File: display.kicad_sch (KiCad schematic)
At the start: 38 parts, among them J301 ConnectorLCDFrontLight, J302 FPC24(0.5MM), J303 FPC10(0.5MM), Q301 2N7002, Q302 2N7002, Q303 AO3401A

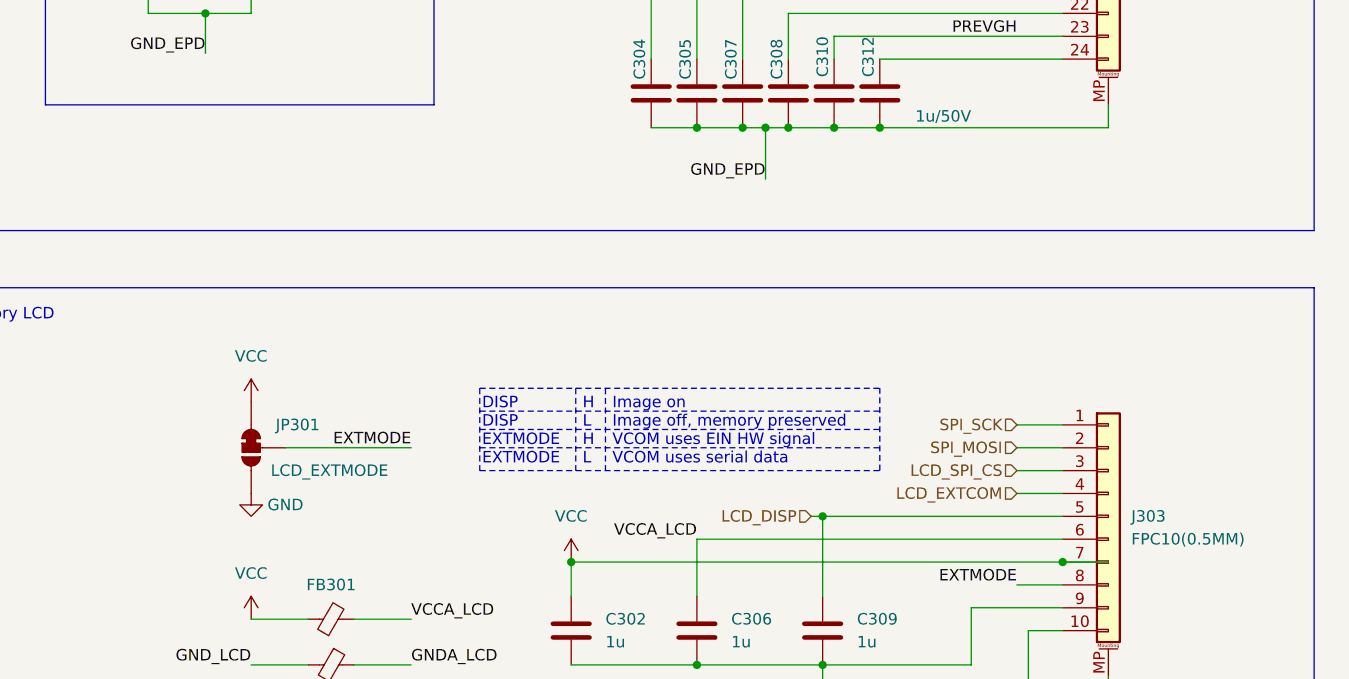
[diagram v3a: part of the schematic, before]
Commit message: schematic: add placeholders for the actual displays
Also fixup GND_LCD for Extmode SolderJumper.
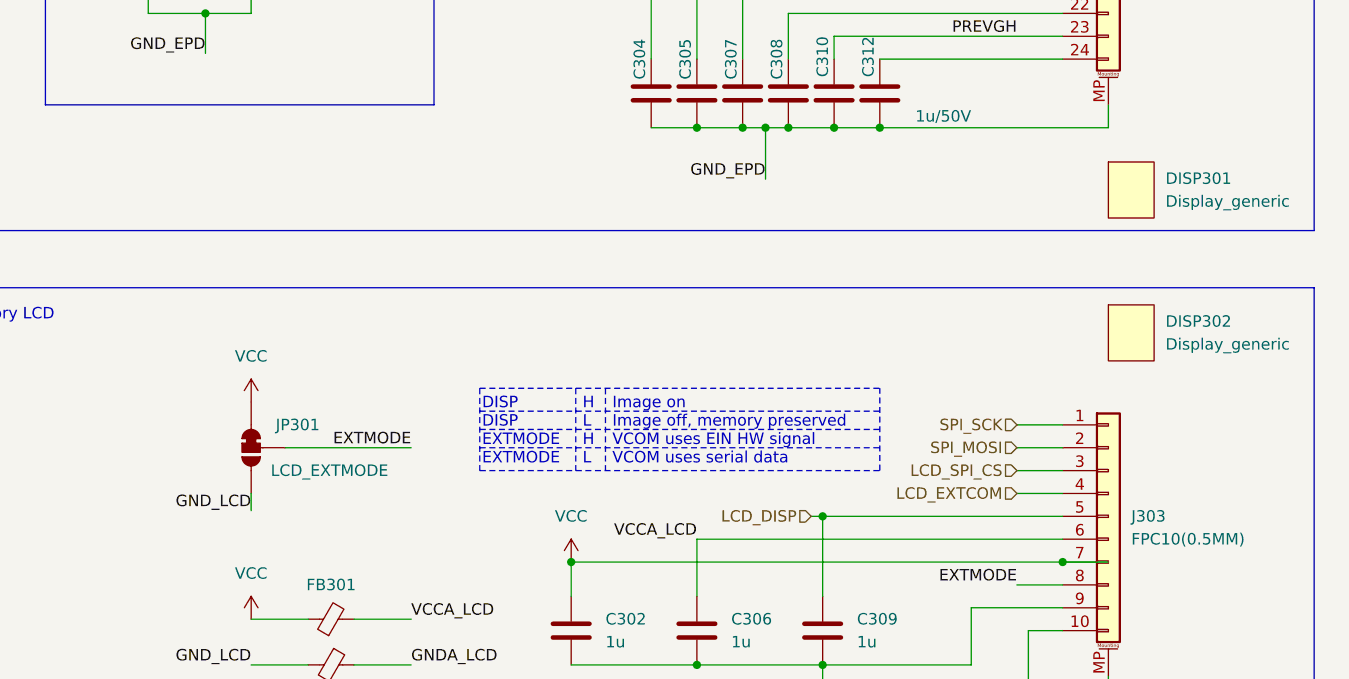
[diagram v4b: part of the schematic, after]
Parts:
- added DISP301, DISP302: Display_generic, project-lib:154_Epaper_Display, symbol project-lib:Display_generic
- J301: JLCPCB (none) -> C11047
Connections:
- net GND: no longer JP301.3 (B)
- net LCD_CURRENT_SENSE: now also JP301.3 (B)
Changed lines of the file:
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@@
+    (stroke (width 0) (type default) (color 0 0 0 0))
+  )
+  (wire (pts (xy 160.02 133.35) (xy 160.02 135.255))
     (stroke (width 0) (type default) (color 0 0 0 0))
   )
@@
   )
   (label "EXTMODE" (at 177.8 128.27 180)
+    (effects (font (size 1.27 1.27)) (justify right bottom))
+  )
+  (label "GND_LCD" (at 160.02 135.255 180)
     (effects (font (size 1.27 1.27)) (justify right bottom))
   )
@@
     )
     (property "Datasheet" "" (id 3) (at 160.02 123.19 0)
-      (effects (font (size 1.27 1.27)) hide)
-    )
-    (pin "1")
-  )
-  (symbol (lib_id "power:GND") (at 160.02 133.35 0) (unit 1)
-    (in_bom yes) (on_board yes)
-    (property "Reference" "#PWR0309" (id 0) (at 160.02 139.7 0)
-      (effects (font (size 1.27 1.27)) hide)
-    )
-    (property "Value" "GND" (id 1) (at 163.83 134.62 0))
-    (property "Footprint" "" (id 2) (at 160.02 133.35 0)
-      (effects (font (size 1.27 1.27)) hide)
-    )
-    (property "Datasheet" "" (id 3) (at 160.02 133.35 0)
       (effects (font (size 1.27 1.27)) hide)
     )
@@
       (effects (font (size 1.27 1.27)) hide)
     )
+    (property "JLCPCB" "C11047" (id 4) (at 102.235 139.7 0)
+      (effects (font (size 1.27 1.27)) hide)
+    )
     (pin "1")
     (pin "2")
@@
     (pin "1")
   )
+  (symbol (lib_id "project-lib:Display_generic") (at 257.81 116.205 0) (unit 1)
+    (in_bom no) (on_board yes) (fields_autoplaced)
+    (property "Reference" "DISP302" (id 0) (at 261.62 114.2364 0)
+      (effects (font (size 1.27 1.27)) (justify left))
+    )
+    (property "Value" "Display_generic" (id 1) (at 261.62 116.7764 0)
+      (effects (font (size 1.27 1.27)) (justify left))
+    )
+    (property "Footprint" "project-lib:154_Epaper_Display" (id 2) (at 257.81 116.205 0)
+      (effects (font (size 1.27 1.27)) hide)
+    )
+    (property "Datasheet" "" (id 3) (at 257.81 116.205 0)
+      (effects (font (size 1.27 1.27)) hide)
+    )
+  )
   (symbol (lib_id "Device:D") (at 171.45 67.31 0) (unit 1)
     (in_bom yes) (on_board yes)
@@
     (pin "1")
   )
+  (symbol (lib_id "project-lib:Display_generic") (at 257.81 100.33 0) (unit 1)
+    (in_bom no) (on_board yes) (fields_autoplaced)
+    (property "Reference" "DISP301" (id 0) (at 261.62 98.3614 0)
+      (effects (font (size 1.27 1.27)) (justify left))
+    )
+    (property "Value" "Display_generic" (id 1) (at 261.62 100.9014 0)
+      (effects (font (size 1.27 1.27)) (justify left))
+    )
+    (property "Footprint" "project-lib:154_Epaper_Display" (id 2) (at 257.81 100.33 0)
+      (effects (font (size 1.27 1.27)) hide)
+    )
+    (property "Datasheet" "" (id 3) (at 257.81 100.33 0)
+      (effects (font (size 1.27 1.27)) hide)
+    )
+  )
   (symbol (lib_id "Transistor_FET:2N7002") (at 90.17 51.435 0) (unit 1)

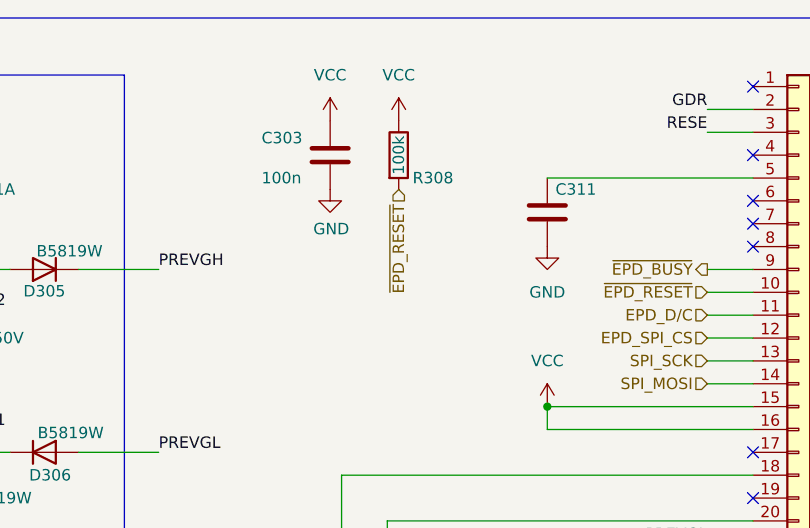
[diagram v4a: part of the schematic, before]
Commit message: schematic: GND_EPD fixups
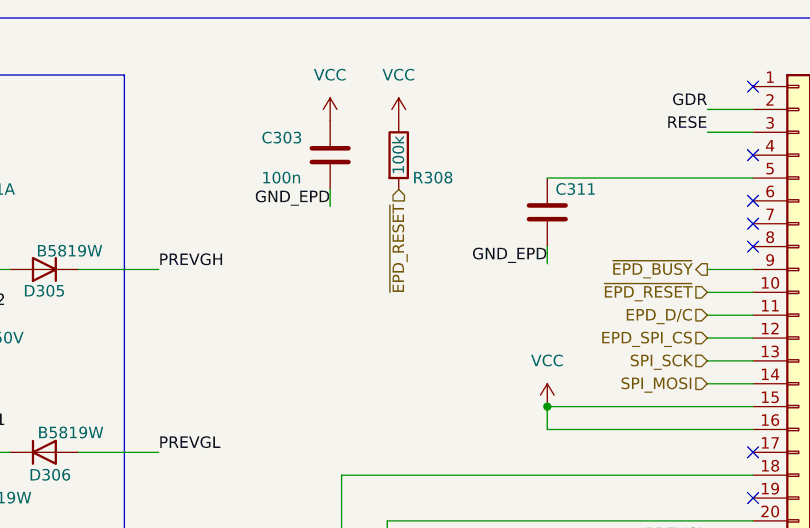
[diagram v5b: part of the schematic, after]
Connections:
- net EPD_CURRENT_SENSE: now also C303.2, C311.2
- net GND: no longer C303.2, C311.2
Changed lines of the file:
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@@
+    (stroke (width 0) (type default) (color 0 0 0 0))
+  )
+  (wire (pts (xy 203.2 38.1) (xy 203.2 40.005))
     (stroke (width 0) (type default) (color 0 0 0 0))
   )
@@
     (stroke (width 0) (type default) (color 0 0 0 0))
   )
+  (wire (pts (xy 227.33 44.45) (xy 227.33 46.355))
+    (stroke (width 0) (type default) (color 0 0 0 0))
+  )
   (wire (pts (xy 219.71 80.01) (xy 250.19 80.01))
     (stroke (width 0) (type default) (color 0 0 0 0))
@@
     (effects (font (size 1.27 1.27)) (justify right bottom))
   )
+  (label "GND_EPD" (at 227.33 46.355 180)
+    (effects (font (size 1.27 1.27)) (justify right bottom))
+  )
   (label "GND_LCD" (at 160.02 135.255 180)
     (effects (font (size 1.27 1.27)) (justify right bottom))
@@
   )
   (label "GND_LCD" (at 62.865 140.97 180)
+    (effects (font (size 1.27 1.27)) (justify right bottom))
+  )
+  (label "GND_EPD" (at 203.2 40.005 180)
     (effects (font (size 1.27 1.27)) (justify right bottom))
   )
@@
     (pin "2")
   )
-  (symbol (lib_id "power:GND") (at 227.33 44.45 0) (unit 1)
-    (in_bom yes) (on_board yes) (fields_autoplaced)
-    (property "Reference" "#PWR0315" (id 0) (at 227.33 50.8 0)
-      (effects (font (size 1.27 1.27)) hide)
-    )
-    (property "Value" "GND" (id 1) (at 227.33 49.53 0))
-    (property "Footprint" "" (id 2) (at 227.33 44.45 0)
-      (effects (font (size 1.27 1.27)) hide)
-    )
-    (property "Datasheet" "" (id 3) (at 227.33 44.45 0)
-      (effects (font (size 1.27 1.27)) hide)
-    )
-    (pin "1")
-  )
   (symbol (lib_id "Device:R") (at 107.315 73.025 0) (unit 1)
     (in_bom yes) (on_board yes) (fields_autoplaced)
@@
     (pin "2")
   )
-  (symbol (lib_id "power:GND") (at 203.2 38.1 0) (unit 1)
-    (in_bom yes) (on_board yes)
-    (property "Reference" "#PWR0313" (id 0) (at 203.2 44.45 0)
-      (effects (font (size 1.27 1.27)) hide)
-    )
-    (property "Value" "GND" (id 1) (at 203.327 42.4942 0))
-    (property "Footprint" "" (id 2) (at 203.2 38.1 0)
-      (effects (font (size 1.27 1.27)) hide)
-    )
-    (property "Datasheet" "" (id 3) (at 203.2 38.1 0)
-      (effects (font (size 1.27 1.27)) hide)
-    )
-    (pin "1")
-  )
   (symbol (lib_id "power:VCC") (at 210.82 30.48 0) (unit 1)

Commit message: footprints: define testpoint with smaller courtyard
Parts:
- TP301, TP302: footprint Connector_PinHeader_1.27mm:PinHeader_1x03_P1.27mm_Vertical -> project-lib:TestPoint_1x03_P1.27mm
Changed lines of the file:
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@@
       (effects (font (size 1.27 1.27)) hide)
     )
-    (property "Footprint" "Connector_PinHeader_1.27mm:PinHeader_1x03_P1.27mm_Vertical" (id 2) (at 48.768 65.405 0)
+    (property "Footprint" "project-lib:TestPoint_1x03_P1.27mm" (id 2) (at 48.768 65.405 0)
       (effects (font (size 1.27 1.27)) hide)
     )
@@
       (effects (font (size 1.27 1.27)) hide)
     )
-    (property "Footprint" "Connector_PinHeader_1.27mm:PinHeader_1x03_P1.27mm_Vertical" (id 2) (at 49.403 135.89 0)
-      (effects (font (size 1.27 1.27)) hide)
-    )
+    (property "Footprint" "project-lib:TestPoint_1x03_P1.27mm" (id 2) (at 49.403 135.89 0)
+      (effects (font (size 1.27 1.27)) hide)
+    )
